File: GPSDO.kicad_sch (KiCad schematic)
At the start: 99 parts, among them J1 Conn_Coaxial, J10 Conn_Coaxial, J2 Barrel_Jack, J3 PROG, J4 DISP_MODULE, J5 GPS_CONN, J6 Conn_Coaxial, J7 Conn_Coaxial, J8 Conn_Coaxial, J9 Conn_Coaxial, SW1 RESET_BTN, U1 REF3440IDBVR, U10 AVR32DB28x-xSO, U11 AZ1117H-5.0TRG1, U12 AZ1117H-5.0TRG1, U13 74HC390, U14 DS34C87T, U15 MCP6486T-E/OT, U2 74AUC2G04, U3 74AUC2G04, U4 74LVC2G74DP,125, U5 AD5680, U6 NB3N551MN, U7 74LVC1G125SE-7, U8 74LVC1G125SE-7, U9 LTC2050IS8, X1 OC5SC25

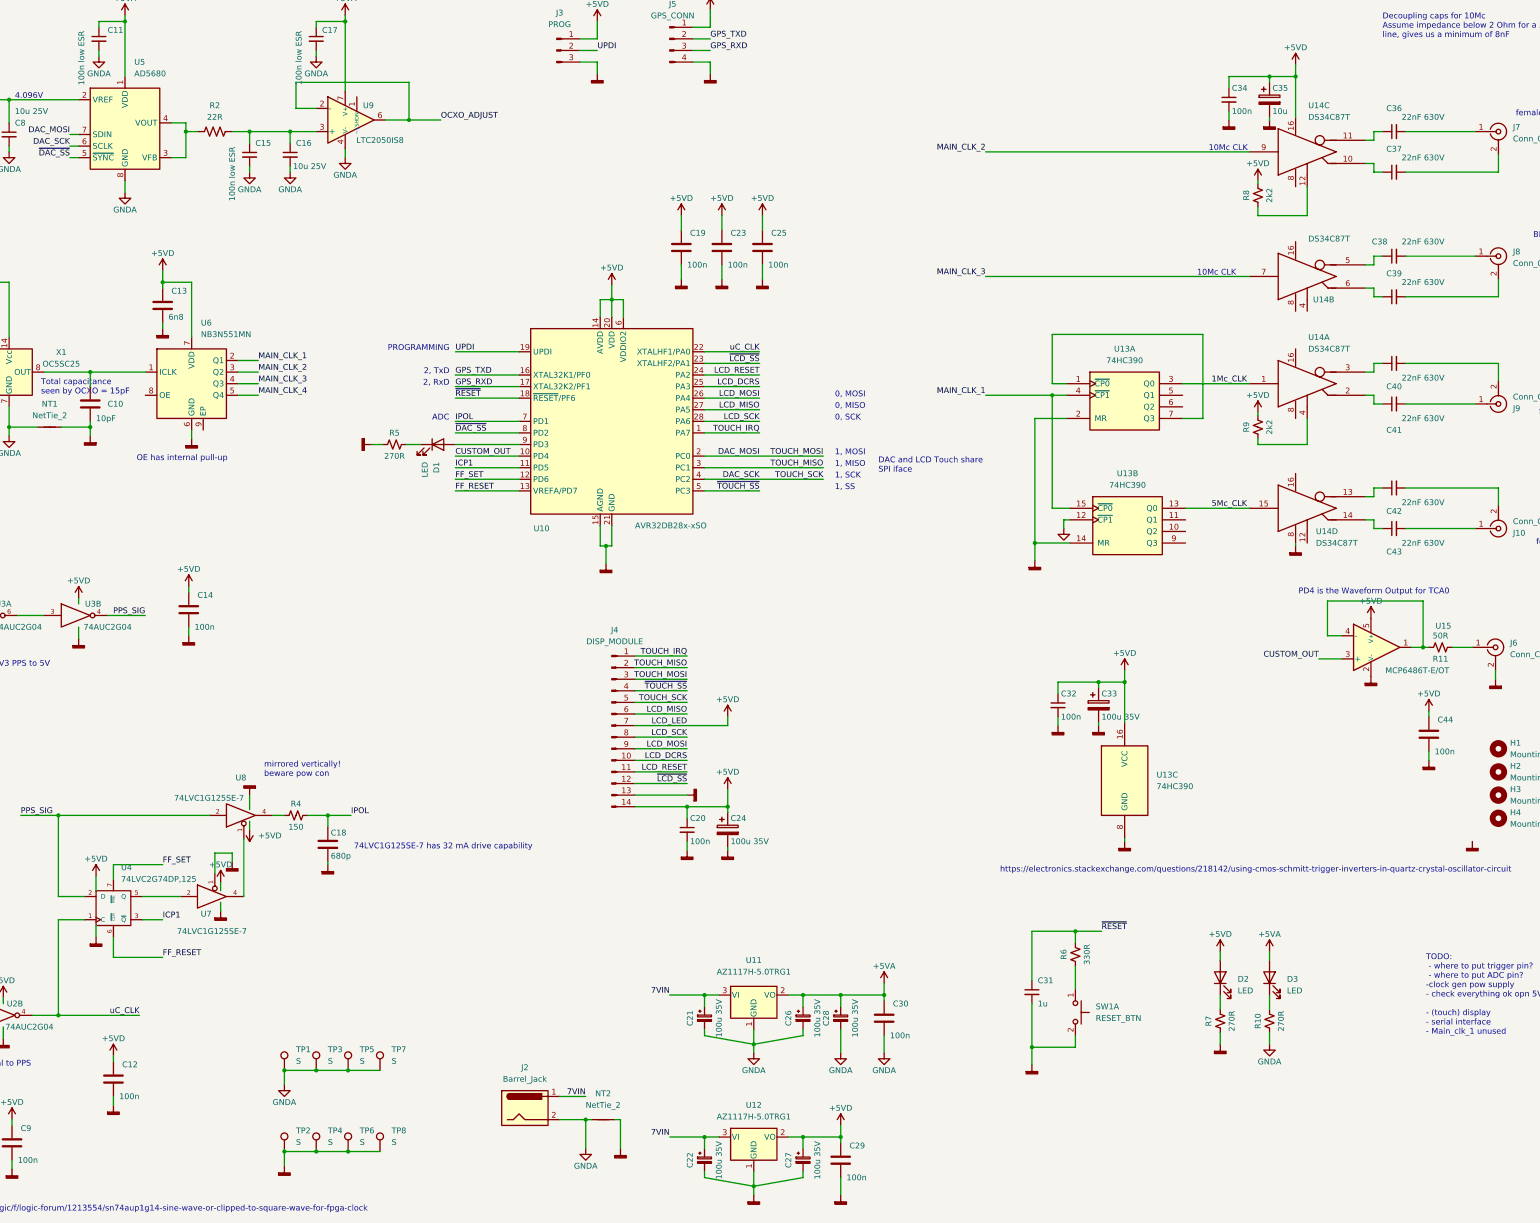
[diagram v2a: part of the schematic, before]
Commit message: changed flipflop & added vref
Flip-flop doesn't really benefit from having a set/reset that can be changed.
uC benefits from having an external reference. If not placed, internal one can be used.
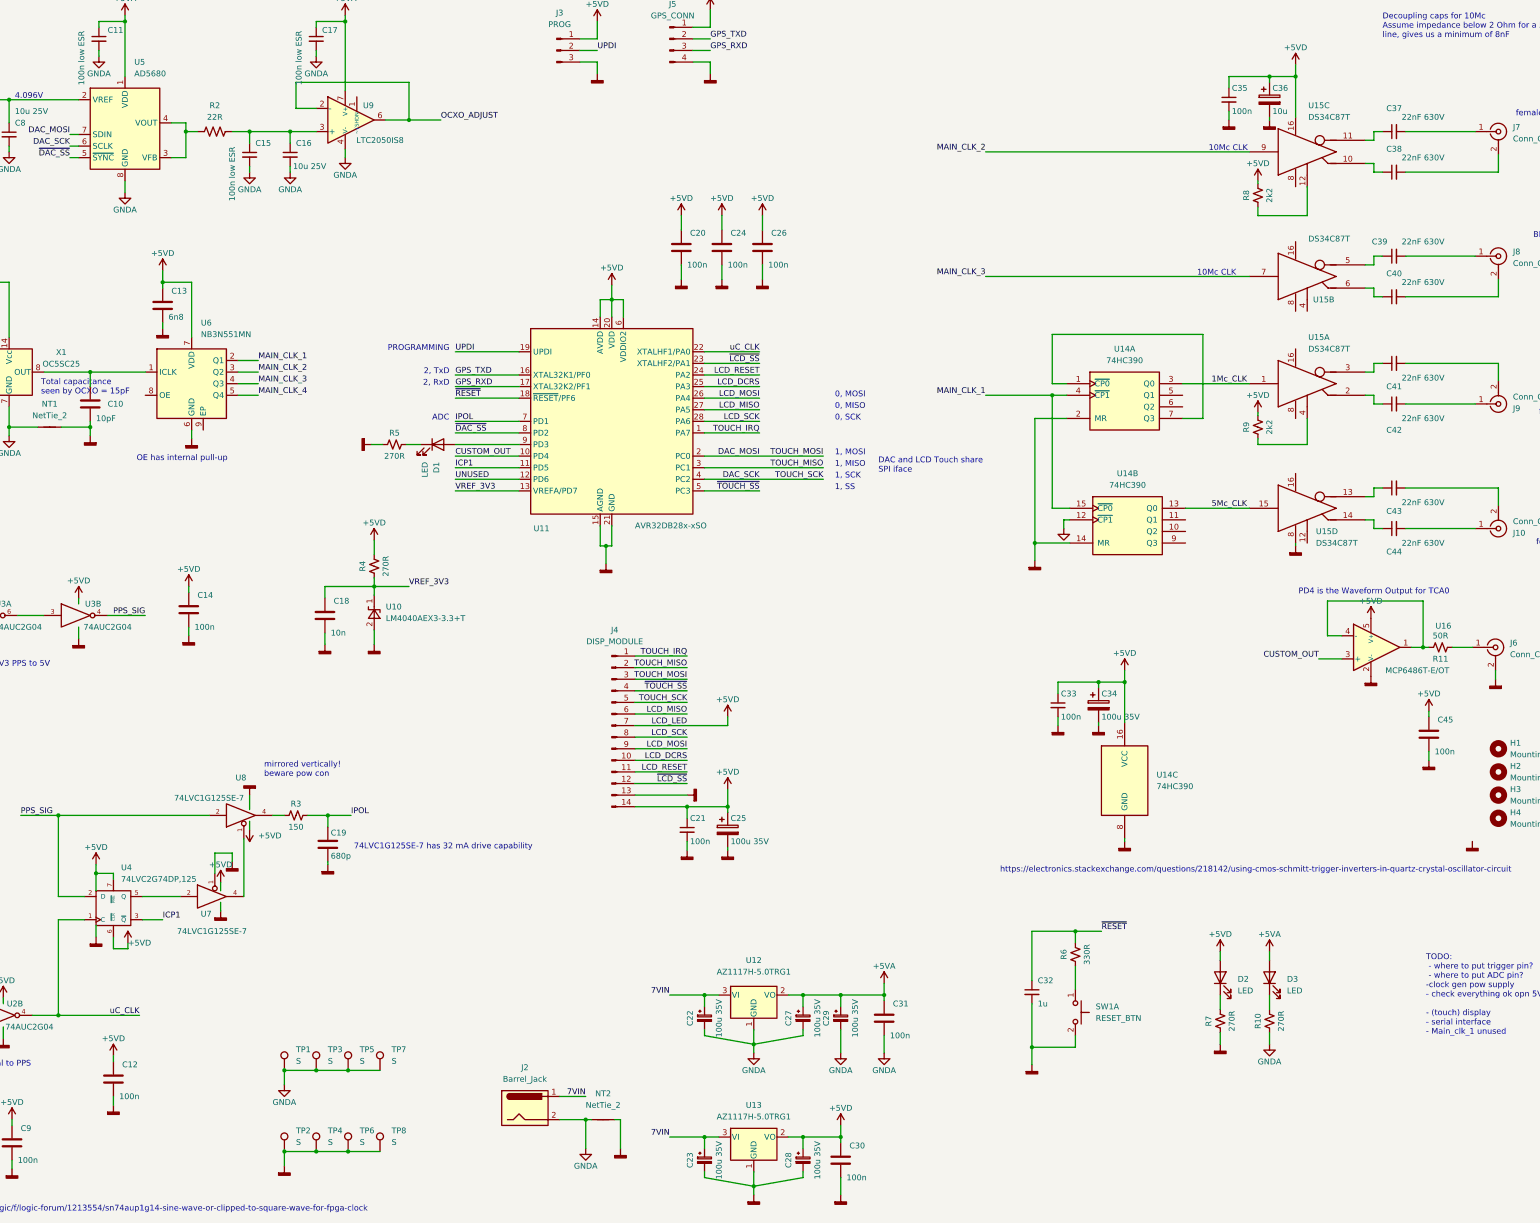
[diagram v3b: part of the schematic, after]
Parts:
- added C18: 10n, Capacitor_SMD:C_0805_2012Metric_Pad1.18x1.45mm_HandSolder, symbol Device:C
- added R4: 270R, Resistor_SMD:R_0805_2012Metric_Pad1.20x1.40mm_HandSolder, symbol Device:R_Small_US
- added U10: LM4040AEX3-3.3+T, Package_TO_SOT_SMD:SOT-23-3, symbol Reference_Voltage:LM4040DBZ-3
- renumbered C18 to C19, C19 to C20, C20 to C21, C21 to C22, C22 to C23, C23 to C24, C24 to C25, C25 to C26, C26 to C27, C27 to C28, C28 to C29, C29 to C30, C30 to C31, C31 to C32, C32 to C33, C33 to C34, C34 to C35, C35 to C36, C36 to C37, C37 to C38, C38 to C39, C39 to C40, C40 to C41, C41 to C42, C42 to C43, C43 to C44, C44 to C45, R4 to R3, U10 to U11, U11 to U12, U12 to U13, U13 to U14, U14 to U15, U15 to U16
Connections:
- net +5VD: now also U4.6 (~{CLR}), U4.7 (~{PRE}), R4.2
- net GND: now also C18.1, U10.2 (A)
- net FF_RESET renamed VREF_3V3
- net VREF_3V3: now also C18.2, R4.1, U10.1 (K); no longer U4.6 (~{CLR})
- net FF_SET renamed UNUSED
- net UNUSED: no longer U4.7 (~{PRE})

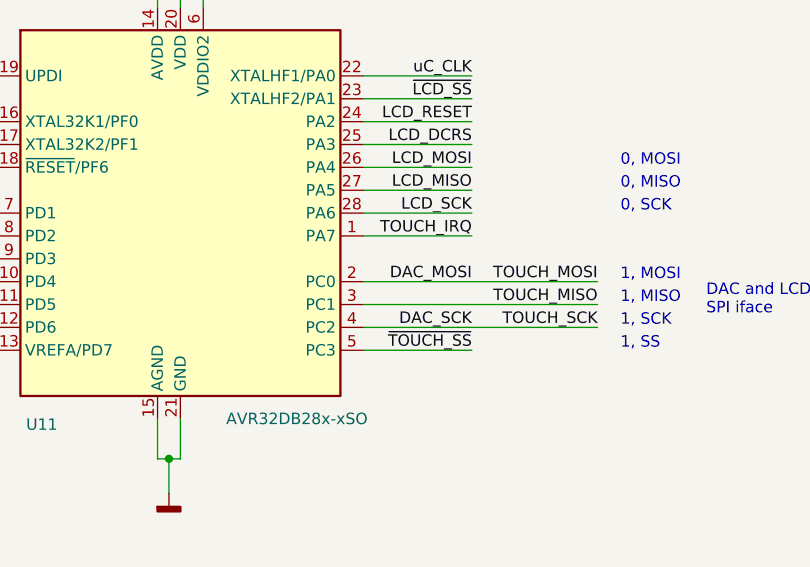
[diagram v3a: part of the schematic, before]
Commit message: updated LCD layout
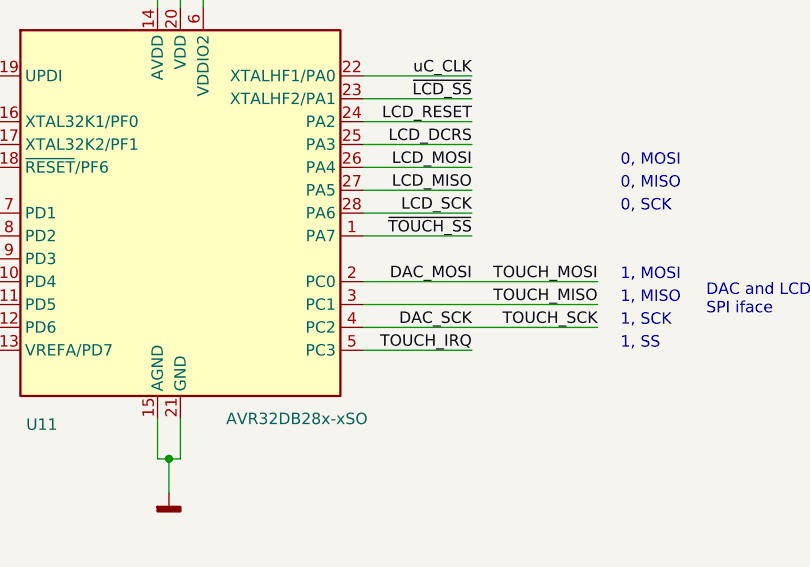
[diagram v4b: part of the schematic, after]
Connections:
- net TOUCH_IRQ: now also U11.5 (PC3); no longer U11.1 (PA7)
- net ~{TOUCH_SS}: now also U11.1 (PA7); no longer U11.5 (PC3)
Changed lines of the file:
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@@
     (effects (font (size 1.27 1.27)) (justify right bottom))
   )
-  (label "TOUCH_IRQ" (at 217.805 111.76 180)
+  (label "TOUCH_IRQ" (at 217.805 124.46 180)
     (effects (font (size 1.27 1.27)) (justify right bottom))
   )
-  (label "~{TOUCH_SS}" (at 217.805 124.46 180)
+  (label "~{TOUCH_SS}" (at 217.805 111.76 180)
     (effects (font (size 1.27 1.27)) (justify right bottom))
   )

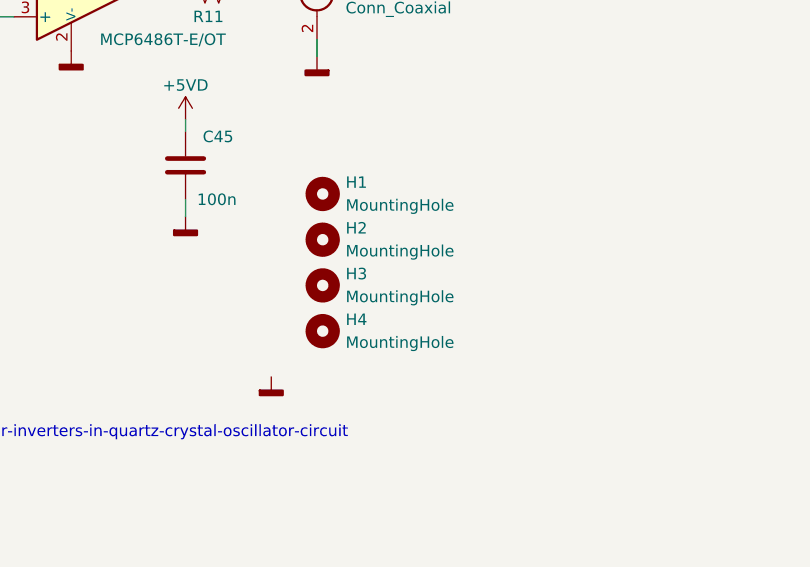
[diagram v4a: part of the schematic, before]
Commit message: updated layout
Added vref footprint
Changed pour params for better gnd coverage
increased digital line distances
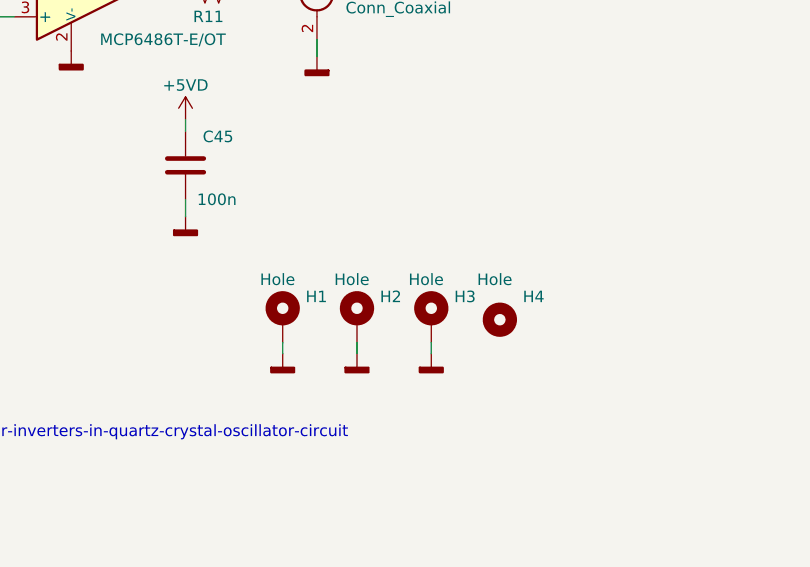
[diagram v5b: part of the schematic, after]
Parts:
- removed H1, H2, H3: MountingHole, MountingHole:MountingHole_3.2mm_M3_Pad, symbol Mechanical:MountingHole
- added H1, H2, H3: Hole, MountingHole:MountingHole_3.2mm_M3_Pad_Via, symbol Mechanical:MountingHole_Pad
- H4: value MountingHole -> Hole
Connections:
- net GND: now also H1.1, H2.1, H3.1

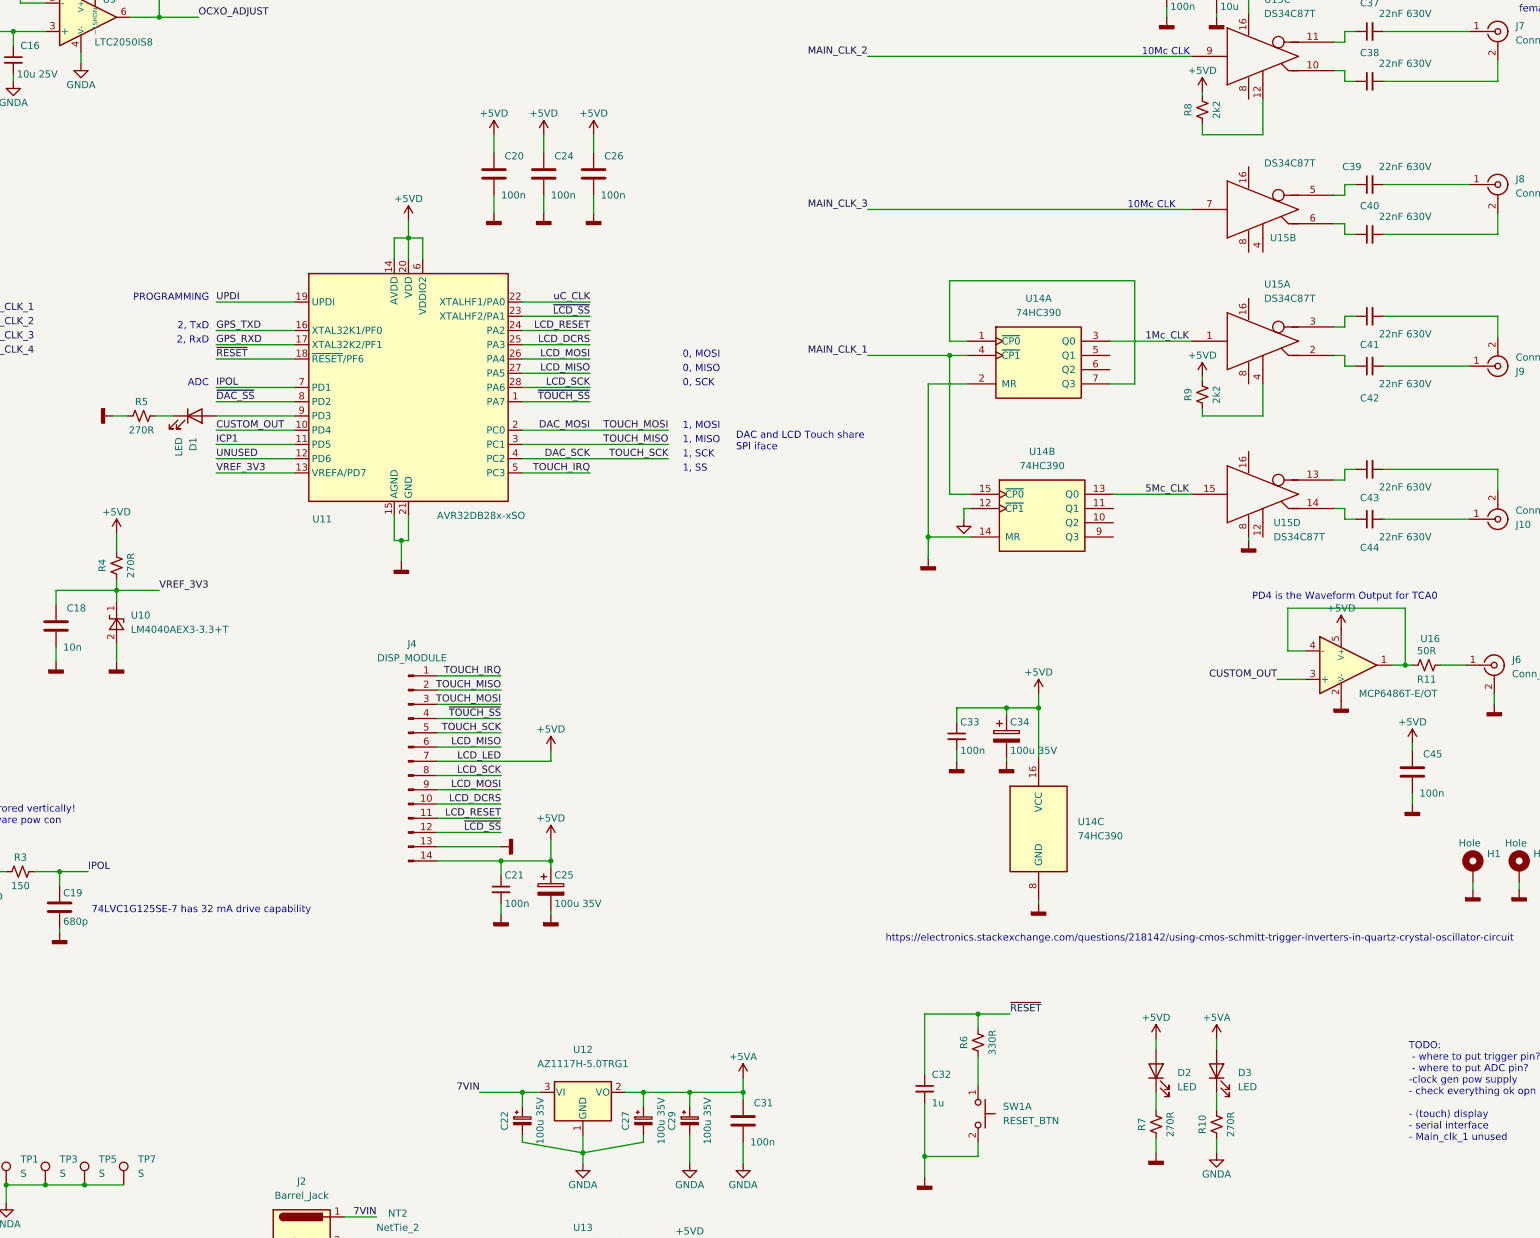
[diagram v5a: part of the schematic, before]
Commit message: Added a second LED to GPIO & layout cleanup
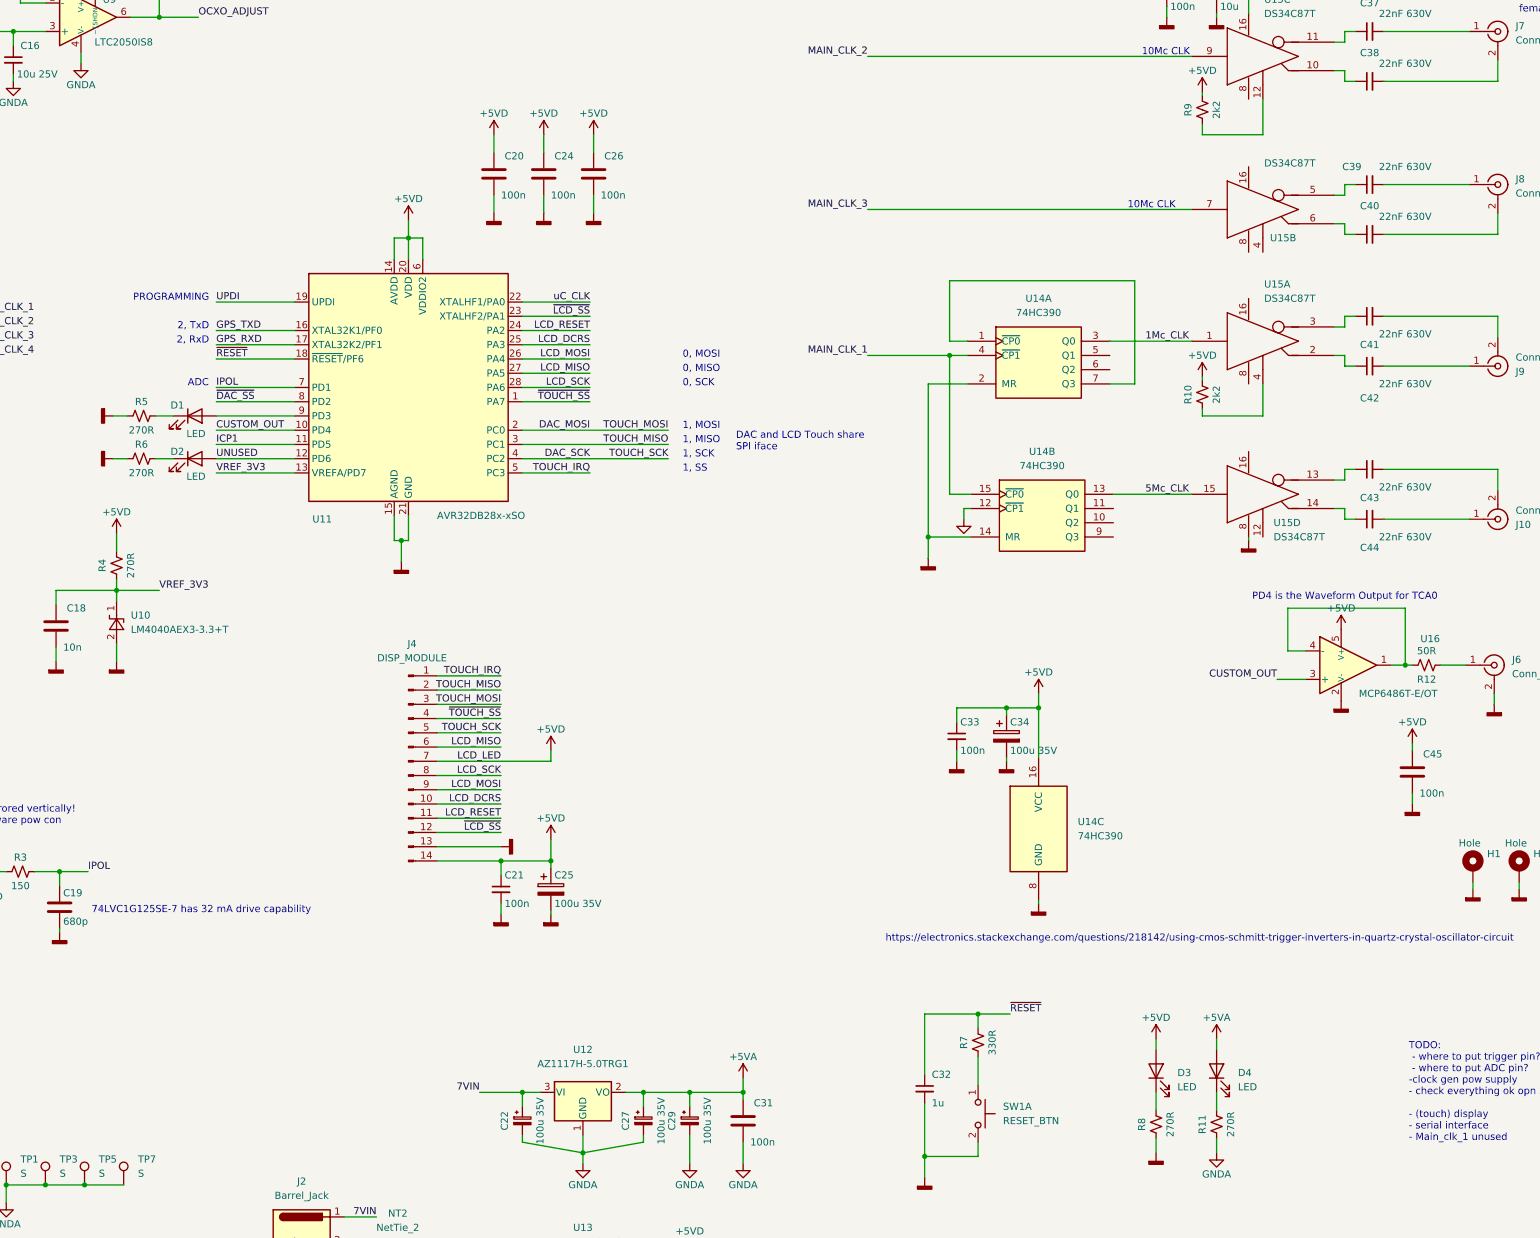
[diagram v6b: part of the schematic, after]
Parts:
- added D2: LED, LED_SMD:LED_0805_2012Metric, symbol Device:LED
- added R6: 270R, Resistor_SMD:R_0805_2012Metric_Pad1.20x1.40mm_HandSolder, symbol Device:R_Small_US
- renumbered D2 to D3, D3 to D4, R9 to R10, R10 to R11, R11 to R12, R6 to R7, R7 to R8, R8 to R9
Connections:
- net GND: now also R6.1
- net UNUSED: now also D2.2 (A)
- new net: D2.1 (K), R6.2
